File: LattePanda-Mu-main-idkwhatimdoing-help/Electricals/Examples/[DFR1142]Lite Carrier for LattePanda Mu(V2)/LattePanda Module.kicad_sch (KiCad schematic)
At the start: 20 parts, among them J1 Conn_01x03_Pin, U18 W25Q128JVS

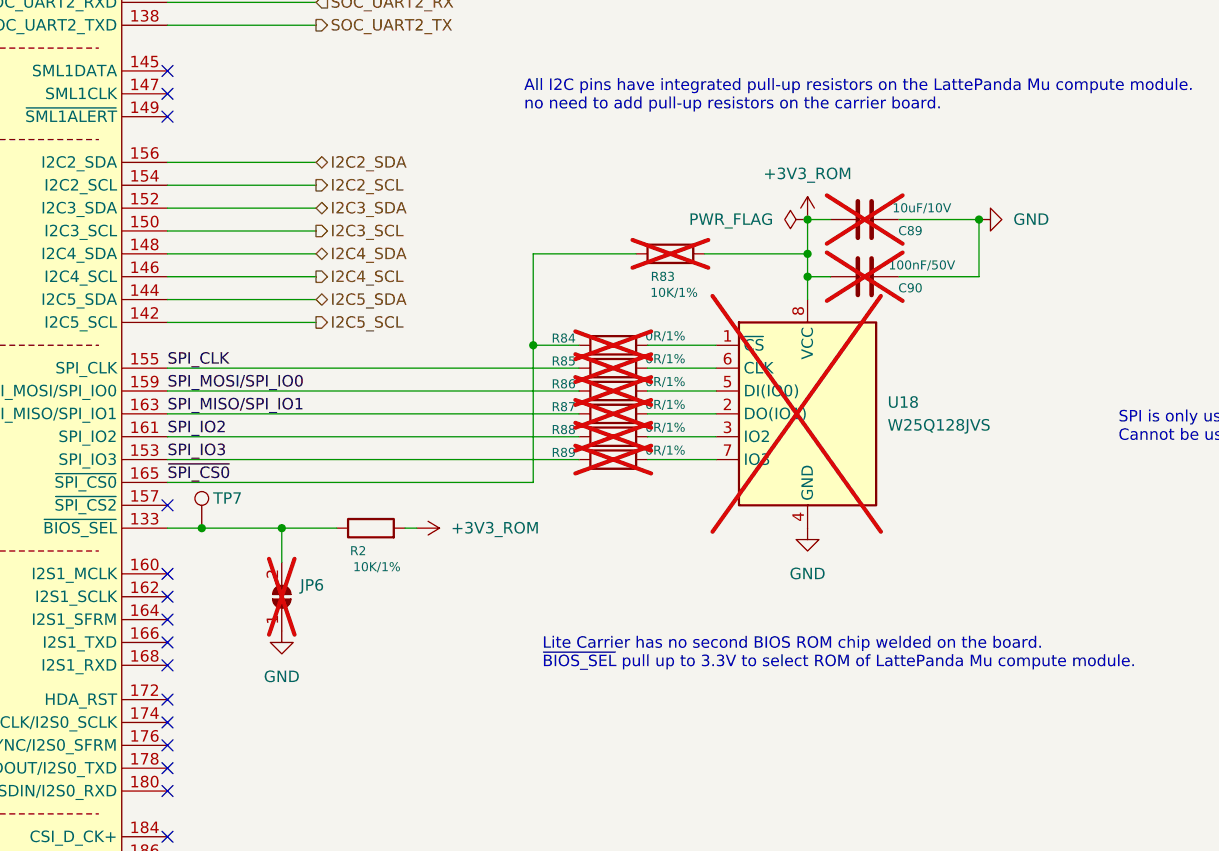
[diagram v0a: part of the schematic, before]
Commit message: Switched Template Carrier board due to issues with the Lattepanda-provided version.
I am not sure what the cause of these "A:DFRobot" missing library footprints are, however the carrier board designed by
youtuber "Ben Makes Everything" has no large changes to the schematic files that I cant handle, and dosen't have this annoying issue. For this reason I
will be using his design as a base. Although I am not using his design directly, I will still link his repository:
https://github.com/BenMakesEverything/Mu_Cyberdeck/tree/main
Thank you BenMakesEverything!
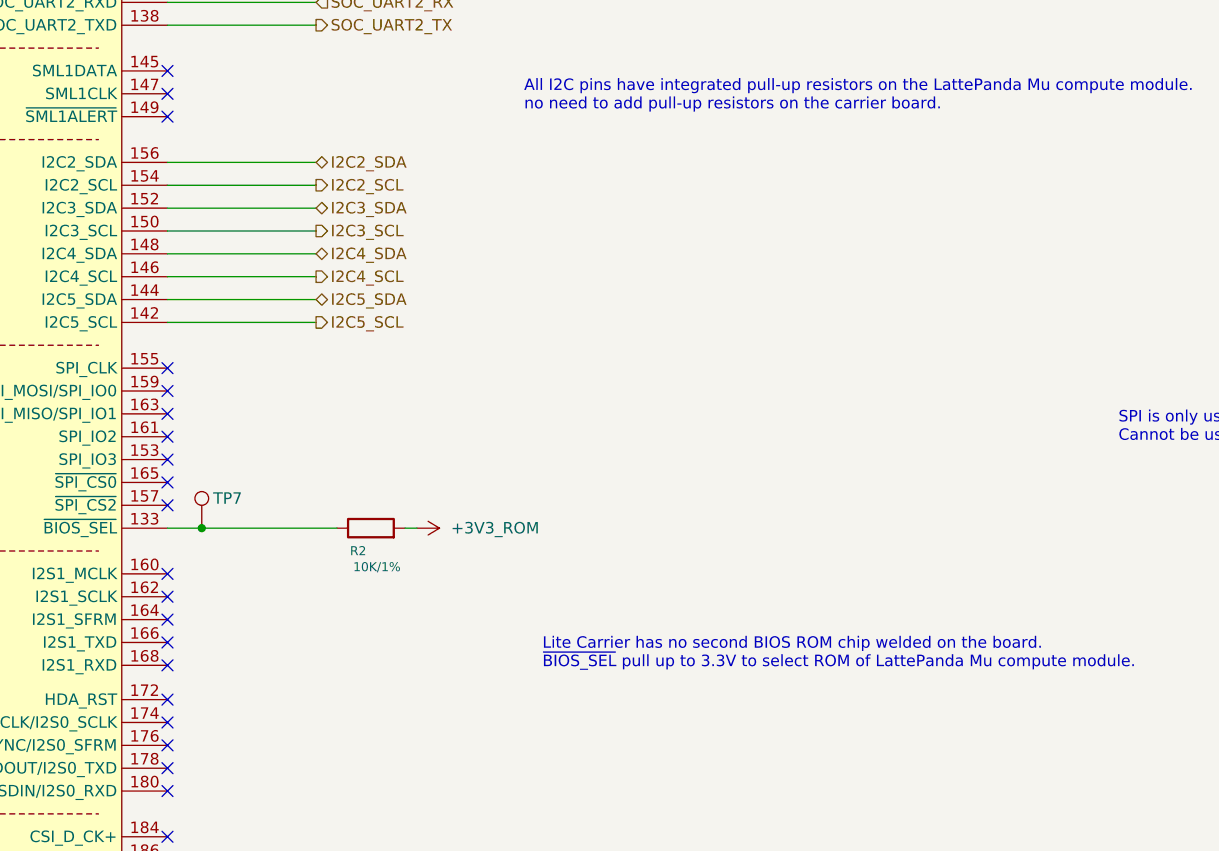
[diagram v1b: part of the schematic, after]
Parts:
- removed C89: 10uF/10V, A_DFRobot:C_0402, symbol Device:C
- removed C90: 100nF/50V, A_DFRobot:C_0402, symbol Device:C
- removed JP6: SolderJumper_2_Open, Jumper:SolderJumper-2_P1.3mm_Open_TrianglePad1.0x1.5mm, symbol Jumper:SolderJumper_2_Open
- removed R83: 10K/1%, A_DFRobot:R_0402, symbol Device:R
- removed R84, R85, R86, R87, R88, R89: 0R/1%, A_DFRobot:R_0402, symbol Device:R
- removed U18: W25Q128JVS, Package_SO:SOIC-8_5.23x5.23mm_P1.27mm, symbol Memory_Flash:W25Q128JVS
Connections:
- net SPI_CLK: no longer names the net of A1.155 (SPI_CLK)
- net SPI_IO2: no longer names the net of A1.161 (SPI_IO2)
- net SPI_IO3: no longer names the net of A1.153 (SPI_IO3)
- net SPI_MISO/SPI_IO1: no longer names the net of A1.163 (SPI_MISO/SPI_IO1)
- net SPI_MOSI/SPI_IO0: no longer names the net of A1.159 (SPI_MOSI/SPI_IO0)
- net ~{SPI_CS0}: no longer names the net of A1.165 (~{SPI_CS0})
- no-connect marks 71 -> 77
